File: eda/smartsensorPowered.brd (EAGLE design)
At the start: 47 x 26.7 mm, 35 parts, among them Q1 IRFML8244, Q2 IRFML8244, Q3 IRFML8244, Q4 IRFML8244, U1 ISL83491SOIC, U2 ATTINY1634

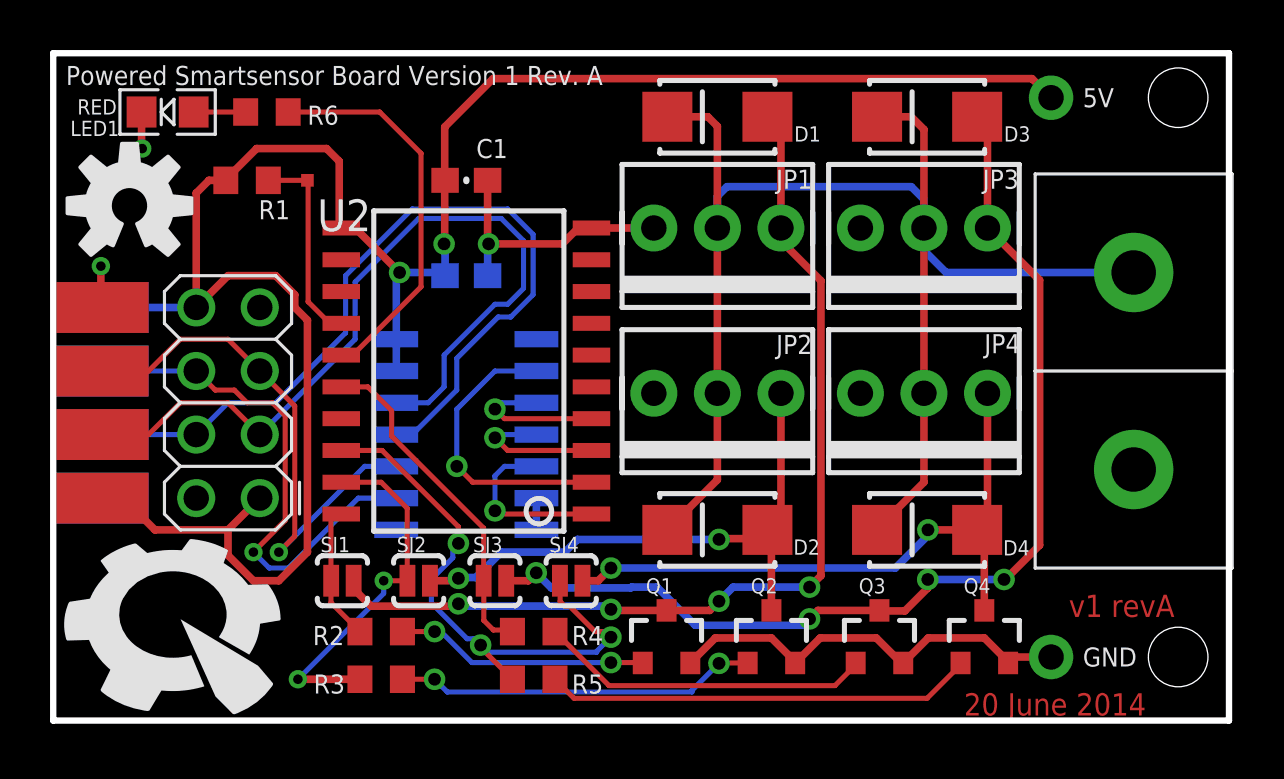
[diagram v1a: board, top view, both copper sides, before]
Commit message: Fixed STANDOFF packages tKeepout.
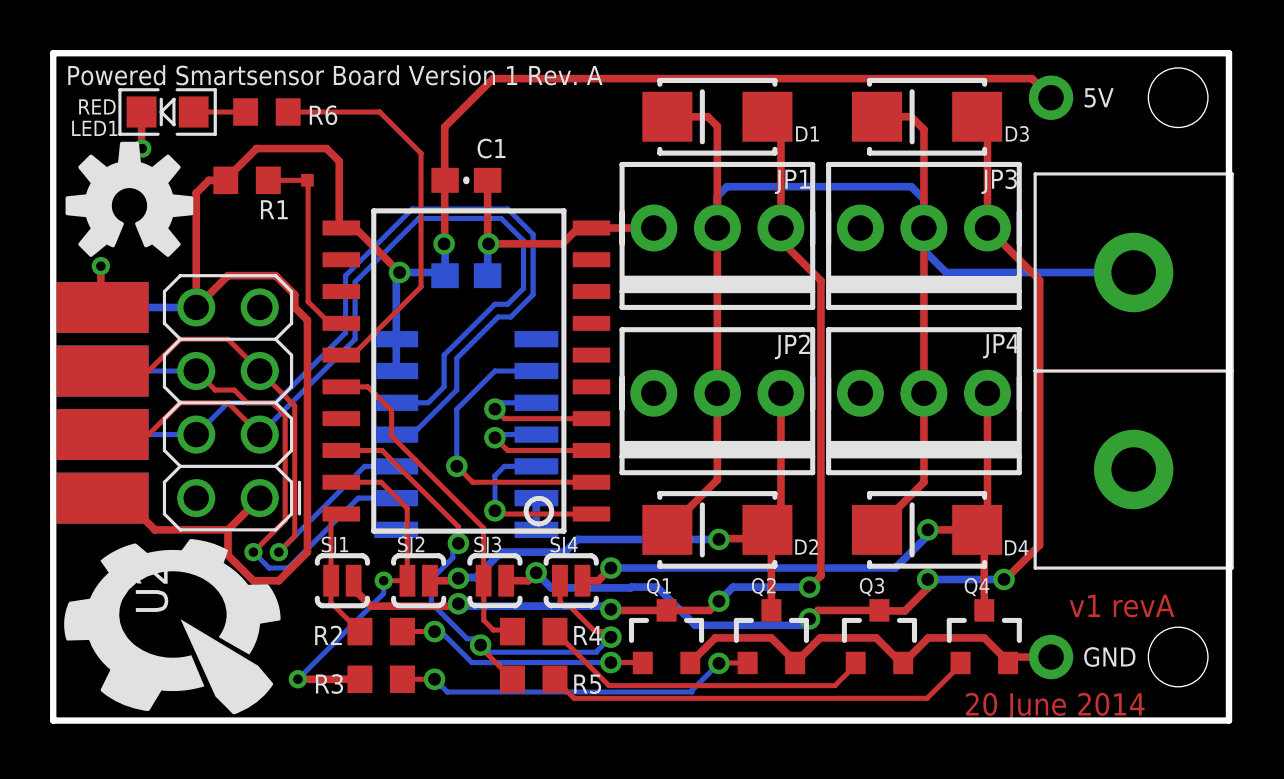
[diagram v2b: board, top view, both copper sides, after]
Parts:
- U2: device pie:SOIC20S -> pie:SOIC20
- moved U2 7.41 mm to (16.5, 14.0), turned to 180 degrees
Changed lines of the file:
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@@
 <setting verticaltext="up"/>
 </settings>
-<grid distance="0.05" unitdist="inch" unit="inch" style="lines" multiple="1" display="yes" altdistance="0.005" altunitdist="inch" altunit="inch"/>
+<grid distance="0.025" unitdist="inch" unit="inch" style="lines" multiple="1" display="yes" altdistance="0.005" altunitdist="inch" altunit="inch"/>
 <layers>
 <layer number="1" name="Top" color="4" fill="1" visible="yes" active="yes"/>
@@
 <attribute name="VALUE" x="20.701" y="16.256" size="0.8128" layer="28" font="vector" ratio="16" rot="MR0"/>
 </element>
-<element name="U2" library="pie" package="SOIC20S" value="ATTINY1634" x="20.32" y="7.62" smashed="yes" rot="R90">
-<attribute name="PIE-INT-REF-NUM" value="ATtiny1634" x="20.32" y="7.62" size="1.778" layer="27" rot="R90" display="off"/>
-<attribute name="NAME" x="12.7" y="20.828" size="1.27" layer="25" ratio="15" rot="R180"/>
-<attribute name="VALUE" x="13.335" y="17.018" size="1.016" layer="27" ratio="16" rot="R270"/>
+<element name="U2" library="pie" package="SOIC20" value="ATTINY1634" x="16.51" y="13.97" smashed="yes" rot="R180">
+<attribute name="PIE-INT-REF-NUM" value="ATtiny1634" x="16.51" y="13.97" size="1.778" layer="27" rot="R180" display="off"/>
+<attribute name="NAME" x="3.302" y="6.35" size="1.27" layer="25" ratio="15" rot="R270"/>
+<attribute name="VALUE" x="7.112" y="6.985" size="1.016" layer="27" ratio="16"/>
 </element>
 <element name="C1" library="pie" package="0603-CAP" value="0.1 uF" x="16.51" y="21.59" smashed="yes">

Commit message: Fixed version of Krystyn ribboncable change
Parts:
- renumbered U$7 to U$12, U$8 to U$13
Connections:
- net 5V: now also U$12.3, U$12.6; no longer U$12.1, U$12.8
- net A_N: now also U$12.2; no longer U$12.4
- net A_P: now also U$12.1; no longer U$12.3
- net B_N: now also U$12.7; no longer U$12.5
- net B_P: now also U$12.8; no longer U$12.6
- net GND: now also U$12.4, U$12.5; no longer U$12.2, U$12.7
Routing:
- net 5V: track 86.2 -> 14.2 mm
- net A_P: track 32.9 -> 15.5 mm
- net A_N: track 33.7 -> 20.5 mm, vias 0 -> 1
- net B_N: track 21.6 -> 17.7 mm
- net B_P: track 21.2 -> 18.7 mm, vias 1 -> 3
- net TXE: track 5.96 -> 5.32 mm
- net TX: track 7.12 -> 6.49 mm
- net RX: track 11.7 -> 11.1 mm
- net !RXE: track 5.88 -> 5.25 mm
- net LED: track 15.6 -> 16.3 mm
- net IO3: track 13.8 -> 14.4 mm
- net IO4: track 23.4 -> 24.0 mm
- net IO2: track 14.7 -> 15.4 mm
- added copper zone on layer 1, net 5V

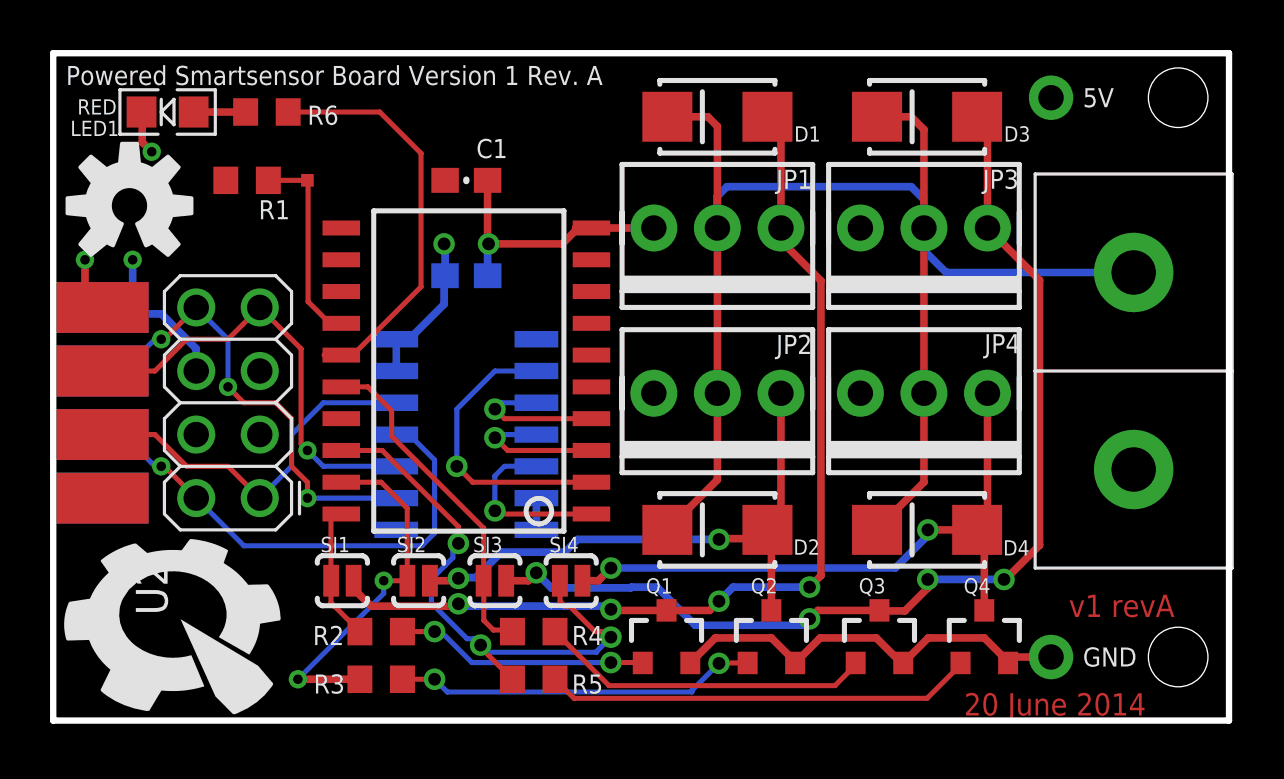
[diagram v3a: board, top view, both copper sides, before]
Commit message: Fixed ribboncable pinout (correctly!)
On battery_buzzer, smartsensor, smartsensor_Powered, team_flag, controller, and grizzly_bear.
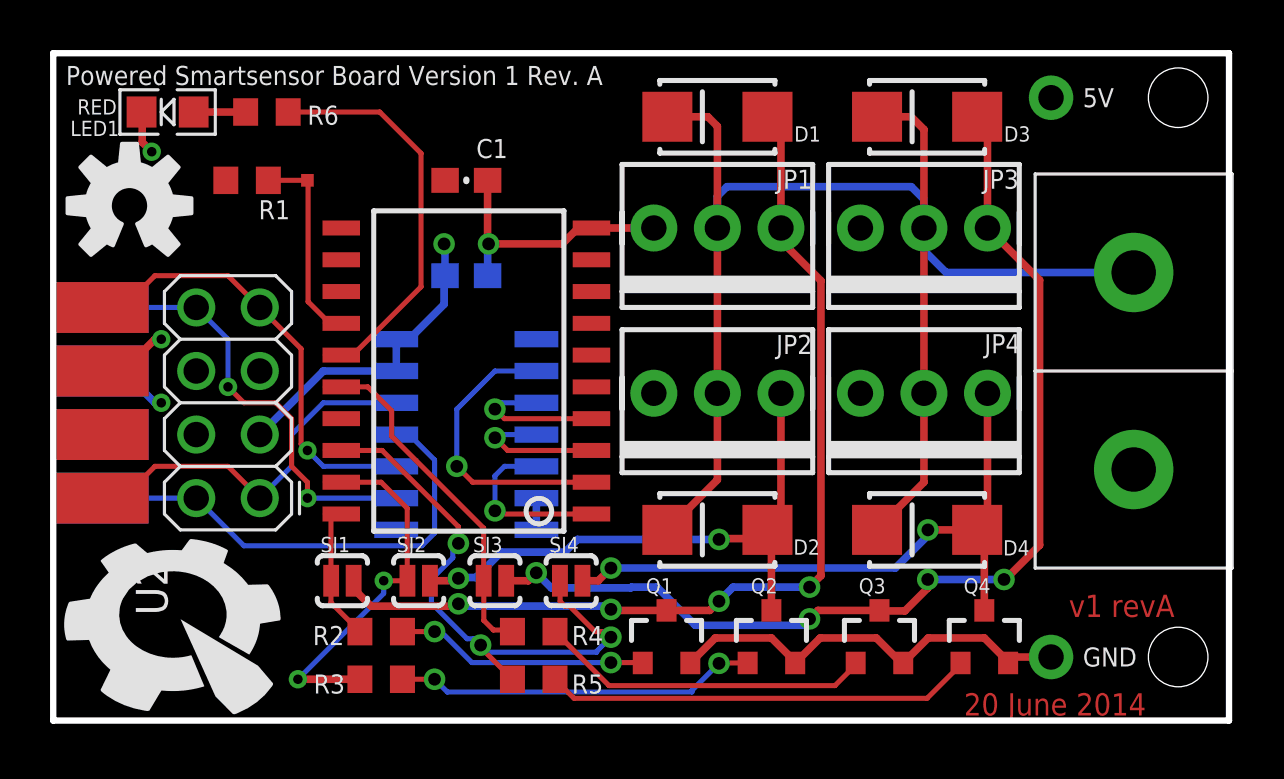
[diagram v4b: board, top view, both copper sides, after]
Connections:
- net 5V: now also U$13.3, U$13.6; no longer U$13.1, U$13.8
- net A_N: now also U$13.2; no longer U$13.4
- net A_P: now also U$13.1; no longer U$13.3
- net B_N: now also U$13.7; no longer U$13.5
- net B_P: now also U$13.8; no longer U$13.6
- net GND: now also U$13.4, U$13.5; no longer U$13.2, U$13.7
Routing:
- net 5V: track 14.2 -> 16.2 mm
- net A_N: track 20.5 -> 19.2 mm, vias 1 -> 0
- net B_P: track 18.7 -> 17.6 mm, vias 3 -> 2
- net TXE: track 5.32 -> 5.96 mm
- net TX: track 6.49 -> 7.12 mm
- net RX: track 11.1 -> 11.7 mm
- net !RXE: track 5.25 -> 5.88 mm

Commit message: All jigs probe vias accessible after populating.
Also changed "VCC" signal name on jigs to "5V" to match boards.
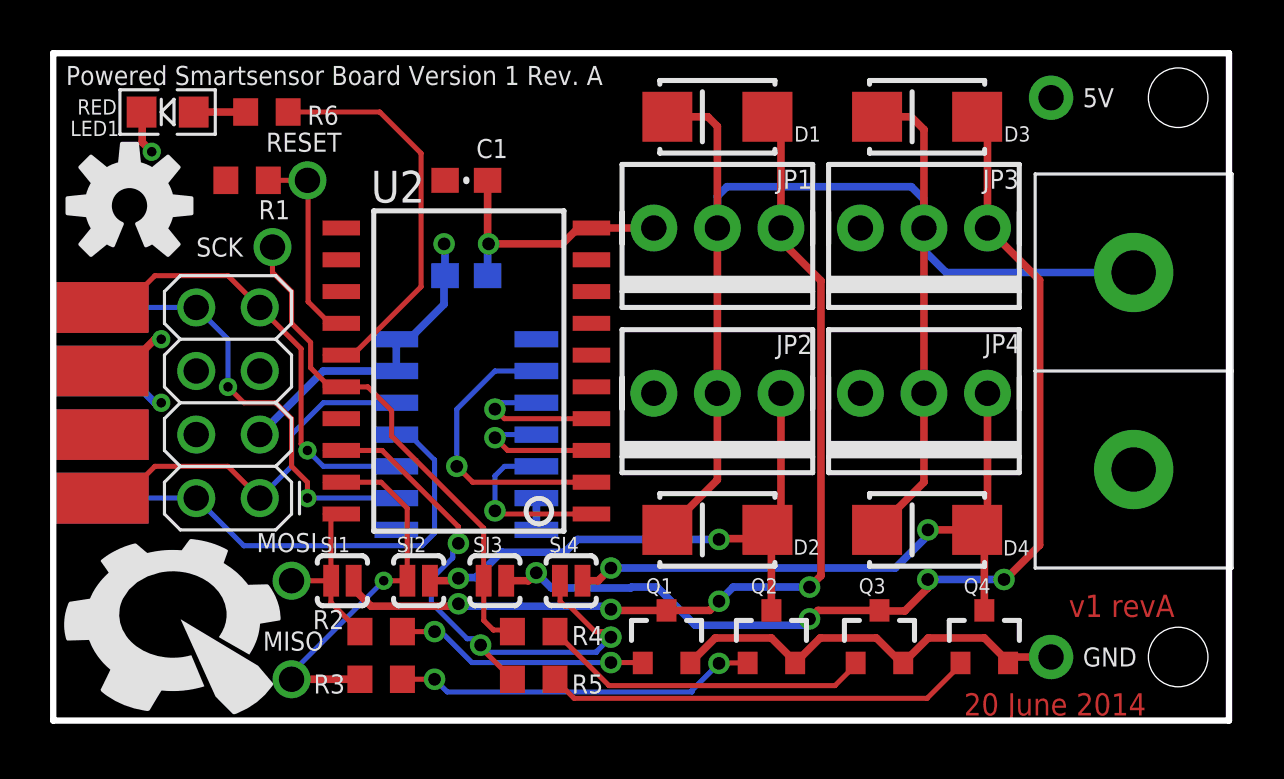
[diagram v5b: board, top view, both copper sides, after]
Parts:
- removed TP1: TEST-POINT2, pie:PAD.02X.02
- added MISO, MOSI, RESET, SCK: (no value), pie:POGO_PIN_394
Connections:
- net IO1: now also MOSI.POGO_PIN
- net IO2: now also MISO.POGO_PIN
- net IO3: now also SCK.POGO_PIN
- net RESET: now also RESET.POGO_PIN; no longer TP1.P$1
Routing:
- net IO3: track 14.4 -> 20.9 mm
- net IO1: track 5.92 -> 7.50 mm
- net IO2: track 15.4 -> 15.7 mm, vias 2 -> 1
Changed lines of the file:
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@@
 <element name="U2" library="pie" package="SOIC20" value="ATTINY1634" x="16.51" y="13.97" smashed="yes" rot="R180">
 <attribute name="PIE-INT-REF-NUM" value="ATtiny1634" x="16.51" y="13.97" size="1.778" layer="27" rot="R180" display="off"/>
-<attribute name="NAME" x="3.302" y="6.35" size="1.27" layer="25" ratio="15" rot="R270"/>
-<attribute name="VALUE" x="7.112" y="6.985" size="1.016" layer="27" ratio="16"/>
+<attribute name="NAME" x="12.7" y="20.701" size="1.27" layer="25" ratio="15"/>
+<attribute name="VALUE" x="14.605" y="8.382" size="1.016" layer="27" ratio="16" rot="R90"/>
 </element>
 <element name="C1" library="pie" package="0603-CAP" value="0.1 uF" x="16.51" y="21.59" smashed="yes">
@@
 <attribute name="PIE-INT-REF-NUM" value="DNL" x="42.418" y="24.892" size="1.778" layer="27" display="off"/>
 <attribute name="NAME" x="41.148" y="24.511" size="0.762" layer="25" ratio="20"/>
-</element>
-<element name="TP1" library="pie" package="PAD.02X.02" value="TEST-POINT2" x="10.16" y="21.59" smashed="yes">
-<attribute name="PIE-INT-REF-NUM" value="DNL" x="10.16" y="21.59" size="1.778" layer="27" display="off"/>
 </element>
 <element name="U$10" library="pie" package="OSHW-LOGO-M" value="" x="3.048" y="20.574"/>
@@
 <element name="R2" library="pie" package="R0603" value="1k" x="13.1064" y="3.556" smashed="yes">
 <attribute name="PIE-INT-REF-NUM" value="RESISTOR-GENERIC" x="13.1064" y="3.556" size="1.778" layer="27" display="off"/>
-<attribute name="NAME" x="10.3759" y="3.01625" size="0.762" layer="25" font="vector" ratio="20"/>
+<attribute name="NAME" x="10.3759" y="3.65125" size="0.762" layer="25" font="vector" ratio="20"/>
 </element>
 <element name="Q2" library="pie" package="SOT23-3" value="IRFML8244" x="28.702" y="3.302" smashed="yes">
@@
 <element name="U$13" library="pie" package="2X4-EDGE" value="SENSOR_CONSMD-EDGE" x="-0.635" y="12.7" smashed="yes" rot="R180">
 <attribute name="PIE-INT-REF-NUM" value="BULK-STOCK" x="-0.635" y="24.13" size="1.778" layer="27" rot="R180" display="off"/>
+</element>
+<element name="RESET" library="pie" package="POGO_PIN_394" value="" x="10.16" y="21.59" smashed="yes">
+<attribute name="PIE-INT-REF-NUM" value="POGO-PIN" x="10.16" y="21.59" size="1.778" layer="27" display="off"/>
+<attribute name="NAME" x="8.509" y="22.733" size="0.762" layer="25" font="vector" ratio="15"/>
+<attribute name="VALUE" x="8.89" y="19.05" size="1.27" layer="27" font="vector"/>
+</element>
+<element name="MOSI" library="pie" package="POGO_PIN_394" value="" x="9.525" y="5.588" smashed="yes">
+<attribute name="PIE-INT-REF-NUM" value="POGO-PIN" x="9.525" y="5.588" size="1.778" layer="27" display="off"/>
+<attribute name="NAME" x="8.128" y="6.731" size="0.762" layer="25" font="vector" ratio="15"/>
+<attribute name="VALUE" x="8.255" y="3.048" size="1.27" layer="27" font="vector"/>
+</element>
+<element name="MISO" library="pie" package="POGO_PIN_394" value="" x="9.525" y="1.651" smashed="yes">
+<attribute name="PIE-INT-REF-NUM" value="POGO-PIN" x="9.525" y="1.651" size="1.778" layer="27" display="off"/>
+<attribute name="NAME" x="8.382" y="2.794" size="0.762" layer="25" font="vector" ratio="15"/>
+<attribute name="VALUE" x="8.255" y="-0.889" size="1.27" layer="27" font="vector"/>
+</element>
+<element name="SCK" library="pie" package="POGO_PIN_394" value="" x="8.763" y="18.923" smashed="yes">
+<attribute name="PIE-INT-REF-NUM" value="POGO-PIN" x="8.763" y="18.923" size="1.778" layer="27" display="off"/>
+<attribute name="NAME" x="5.715" y="18.542" size="0.762" layer="25" font="vector" ratio="15"/>
+<attribute name="VALUE" x="7.493" y="16.383" size="1.27" layer="27" font="vector"/>
 </element>
 </elements>
@@
 <contactref element="U2" pad="14"/>
 <contactref element="R1" pad="1"/>
-<contactref element="TP1" pad="P$1"/>
-<wire x1="10.16" y1="21.59" x2="8.597" y2="21.59" width="0.2032" layer="1"/>
 <wire x1="10.875" y1="15.875" x2="11.049" y2="15.875" width="0.2032" layer="1"/>
 <wire x1="11.049" y1="15.875" x2="10.1854" y2="16.7386" width="0.2032" layer="1"/>
 <wire x1="10.1854" y1="16.7386" x2="10.1854" y2="21.5646" width="0.2032" layer="1"/>
-<wire x1="10.1854" y1="21.5646" x2="10.16" y2="21.59" width="0.2032" layer="1"/>
 <wire x1="11.51" y1="15.875" x2="11.049" y2="15.875" width="0.2032" layer="1"/>
+<contactref element="RESET" pad="POGO_PIN"/>
+<wire x1="8.597" y1="21.59" x2="10.16" y2="21.59" width="0.2032" layer="1"/>
+<wire x1="10.1854" y1="21.5646" x2="10.16" y2="21.59" width="0" layer="19" extent="1-1"/>
 </signal>
 <signal name="A_P">
@@
 <wire x1="11.0998" y1="4.7126" x2="12.2564" y2="3.556" width="0.2032" layer="1"/>
 <wire x1="11.3284" y1="8.255" x2="11.51" y2="8.255" width="0.2032" layer="1"/>
+<contactref element="MOSI" pad="POGO_PIN"/>
+<wire x1="9.525" y1="5.588" x2="11.107" y2="5.588" width="0.2032" layer="1"/>
 </signal>
 <signal name="IO2">
@@
 <wire x1="14.1478" y1="8.4836" x2="14.1478" y2="5.5952" width="0.2032" layer="1"/>
 <wire x1="14.1478" y1="5.5952" x2="14.155" y2="5.588" width="0.2032" layer="1"/>
-<wire x1="12.2564" y1="1.651" x2="9.779" y2="1.651" width="0.3048" layer="1"/>
-<via x="9.779" y="1.651" extent="1-16" drill="0.381"/>
+<wire x1="12.2564" y1="1.651" x2="9.525" y2="1.651" width="0.3048" layer="1"/>
 <via x="13.208" y="5.588" extent="1-16" drill="0.381"/>
 <wire x1="14.155" y1="5.588" x2="13.208" y2="5.588" width="0.2032" layer="1"/>
-<wire x1="13.208" y1="5.588" x2="13.208" y2="5.08" width="0.2032" layer="16"/>
-<wire x1="13.208" y1="5.08" x2="9.779" y2="1.651" width="0.2032" layer="16"/>
 <wire x1="10.875" y1="9.525" x2="11.51" y2="9.525" width="0.2032" layer="1"/>
+<contactref element="MISO" pad="POGO_PIN"/>
+<wire x1="9.525" y1="1.651" x2="9.525" y2="1.905" width="0.2032" layer="16"/>
+<wire x1="9.525" y1="1.905" x2="13.208" y2="5.588" width="0.2032" layer="16"/>
 </signal>
 <signal name="IO3">
@@
 <wire x1="13.5255" y1="11.3665" x2="13.5255" y2="12.3825" width="0.2032" layer="1"/>
 <wire x1="10.875" y1="13.335" x2="11.51" y2="13.335" width="0.2032" layer="1"/>
+<contactref element="SCK" pad="POGO_PIN"/>
+<wire x1="8.763" y1="18.923" x2="8.763" y2="17.907" width="0.2032" layer="1"/>
+<wire x1="8.763" y1="17.907" x2="9.525" y2="17.145" width="0.2032" layer="1"/>
+<wire x1="9.525" y1="17.145" x2="9.525" y2="15.875" width="0.2032" layer="1"/>
+<wire x1="9.525" y1="15.875" x2="10.287" y2="15.113" width="0.2032" layer="1"/>
+<wire x1="10.287" y1="15.113" x2="10.287" y2="14.097" width="0.2032" layer="1"/>
+<wire x1="10.875" y1="13.335" x2="10.875" y2="13.509" width="0.2032" layer="1"/>
+<wire x1="10.875" y1="13.509" x2="10.287" y2="14.097" width="0.2032" layer="1"/>
 </signal>
 <signal name="IO4">
